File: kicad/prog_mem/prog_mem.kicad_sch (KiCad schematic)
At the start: 27 parts

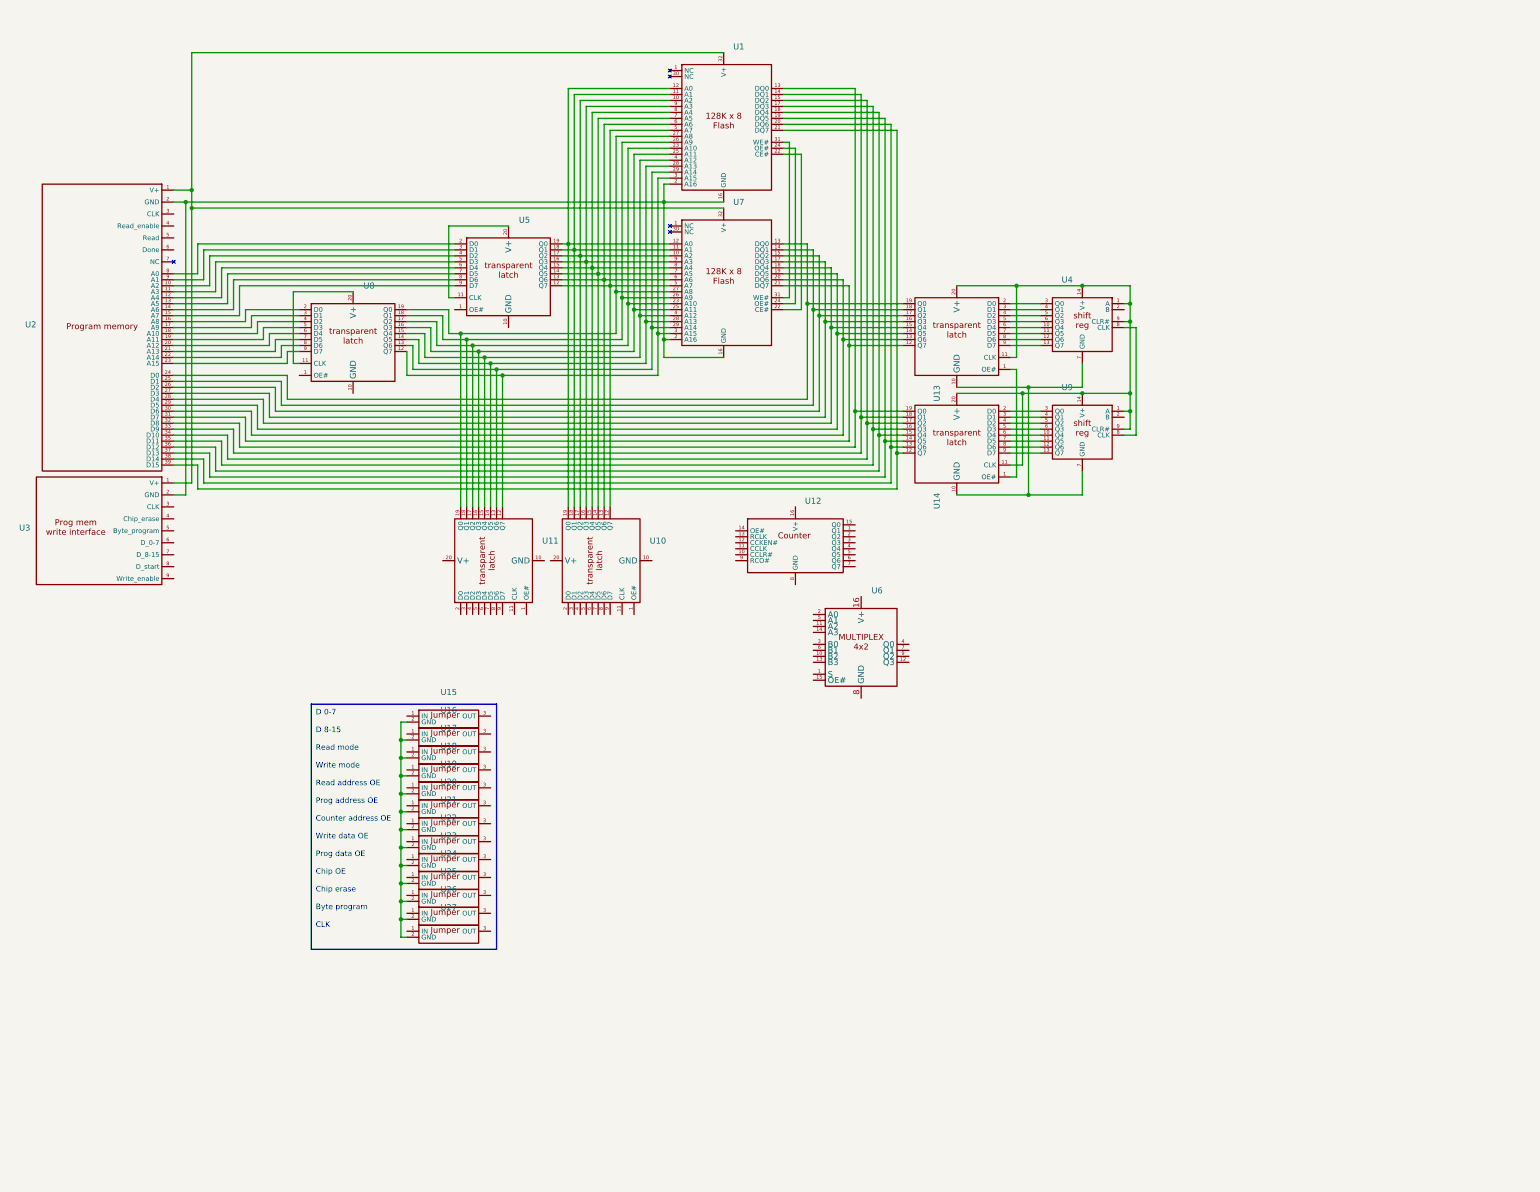
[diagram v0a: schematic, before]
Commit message: Finished some more PCBs and uploaded to JLCPCB
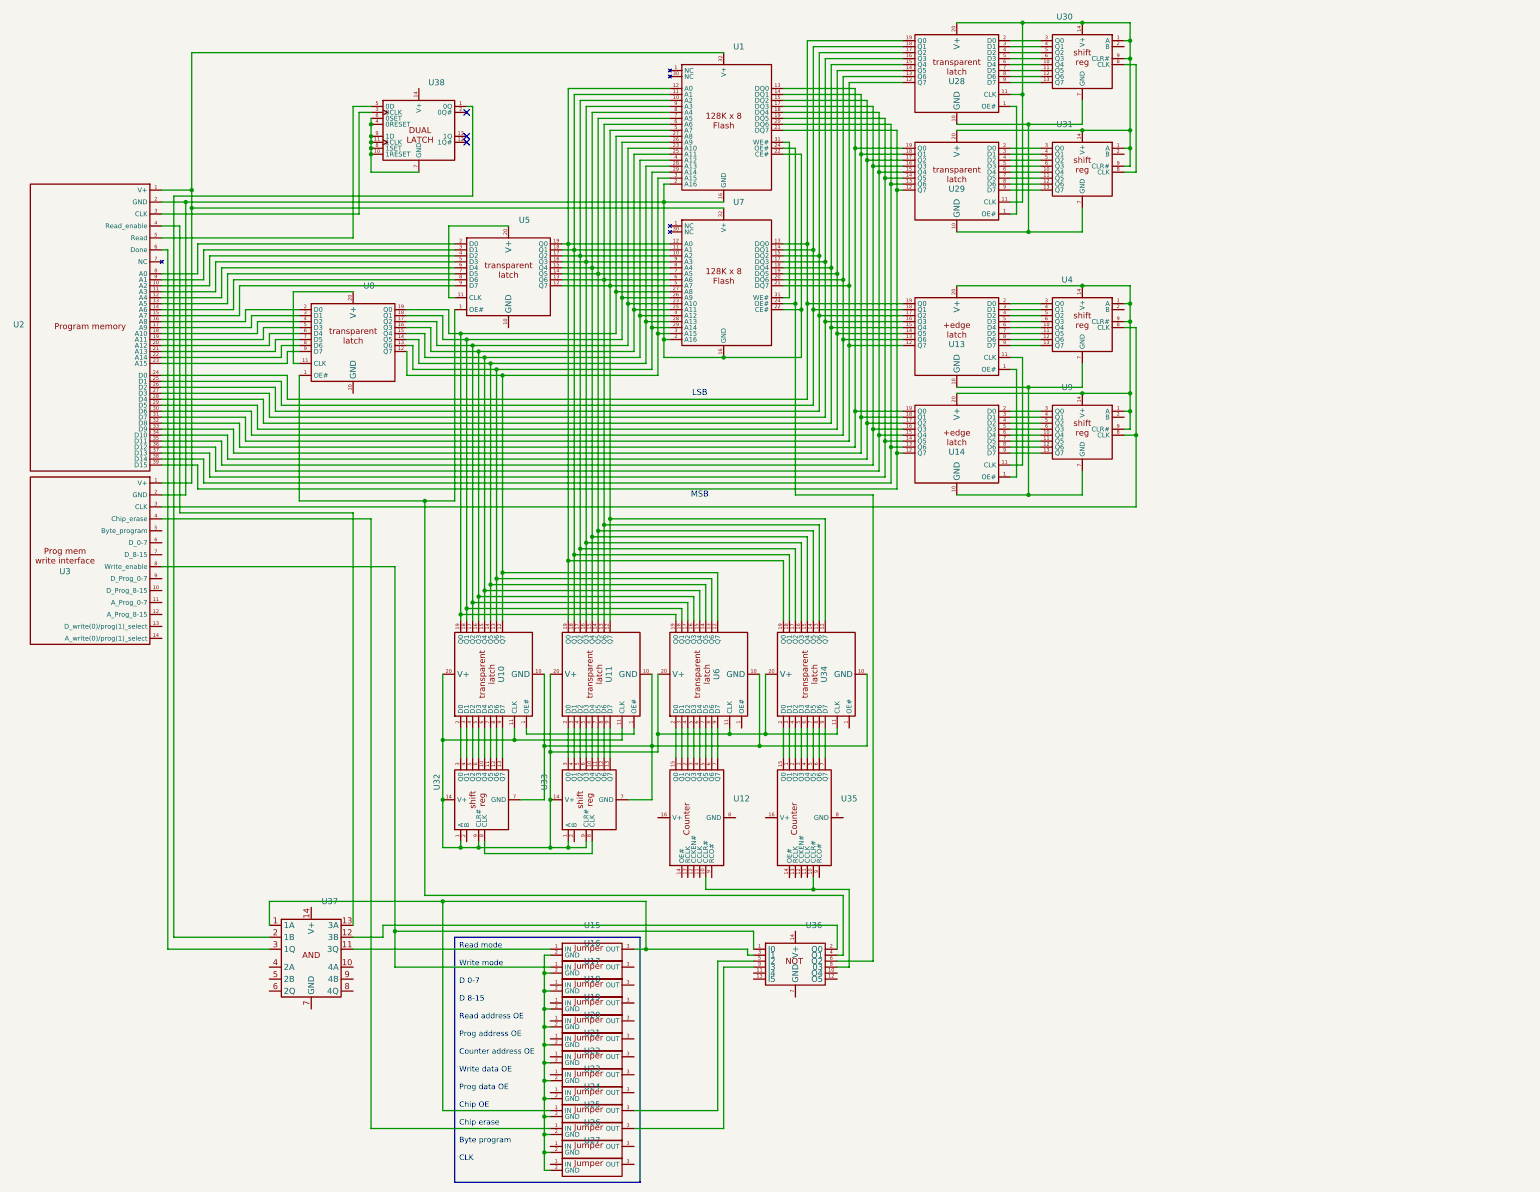
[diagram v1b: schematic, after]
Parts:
- removed U6: ~, Package_DIP:DIP-16_W7.62mm, symbol custom_symbol_lib:2x4_bit_multiplexer
- added U28, U29, U34, U6: ~, Package_DIP:DIP-20_W7.62mm, symbol custom_symbol_lib:8_bit_transparent_latch
- added U30, U31, U32, U33: ~, Package_DIP:DIP-14_W7.62mm, symbol custom_symbol_lib:8_bit_shift_register
- added U35: ~, Package_DIP:DIP-16_W7.62mm, symbol custom_symbol_lib:8_bit_counter
- added U36: ~, Package_DIP:DIP-14_W7.62mm, symbol custom_symbol_lib:6xNOT
- added U37: ~, Package_DIP:DIP-14_W7.62mm, symbol custom_symbol_lib:quad_and
- added U38: ~, Package_DIP:DIP-14_W7.62mm, symbol custom_symbol_lib:dual_latch
- U13, U14: symbol custom_symbol_lib:8_bit_transparent_latch -> custom_symbol_lib:rising_edge_8_bit_latch
- U3: footprint (none) -> Connector_PinHeader_2.54mm:PinHeader_1x08_P2.54mm_Horizontal
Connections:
- net at U12.1 (Q1): now also U6.3 (D1)
- net at U12.10 (CCLR#): now also U35.10 (CCLR#), U36.8 (03)
- net at U12.15 (Q0): now also U6.2 (D0)
- net at U12.2 (Q2): now also U6.4 (D2)
- net at U12.3 (Q3): now also U6.5 (D3)
- net at U12.4 (Q4): now also U6.6 (D4)
- net at U12.5 (Q5): now also U6.7 (D5)
- net at U12.6 (Q6): now also U6.8 (D6)
- net at U12.7 (Q7): now also U6.9 (D7)
- net at U25.1 (IN): now also U3.4 (Chip_erase)
- net at U25.3 (OUT): now also U36.9 (I3)
- net at U10.1 (OE#): now also U11.1 (OE#)
- net at U10.10 (GND): now also U11.10 (GND), U32.7 (GND), U33.7 (GND), U34.10 (GND), U6.10 (GND)
- net at U10.11 (CLK): now also U10.20 (V+), U11.11 (CLK), U11.20 (V+), U32.1 (A), U32.14 (V+), U32.9 (CLR#), U33.1 (A), U33.14 (V+), U33.9 (CLR#), U34.11 (CLK), U34.20 (V+), U6.11 (CLK), U6.20 (V+)
- net at U1.5 (A7), U5.12 (Q7), U7.5 (A7): now also U11.12 (Q7), U34.12 (Q7); no longer U10.12 (Q7)
- net at U1.6 (A6), U5.13 (Q6), U7.6 (A6): now also U11.13 (Q6), U34.13 (Q6); no longer U10.13 (Q6)
- net at U1.7 (A5), U5.14 (Q5), U7.7 (A5): now also U11.14 (Q5), U34.14 (Q5); no longer U10.14 (Q5)
- net at U1.8 (A4), U5.15 (Q4), U7.8 (A4): now also U11.15 (Q4), U34.15 (Q4); no longer U10.15 (Q4)
- net at U1.9 (A3), U5.16 (Q3), U7.9 (A3): now also U11.16 (Q3), U34.16 (Q3); no longer U10.16 (Q3)
- net at U1.10 (A2), U5.17 (Q2), U7.10 (A2): now also U11.17 (Q2), U34.17 (Q2); no longer U10.17 (Q2)
- net at U1.11 (A1), U5.18 (Q1), U7.11 (A1): now also U11.18 (Q1), U34.18 (Q1); no longer U10.18 (Q1)
- net at U1.12 (A0), U5.19 (Q0), U7.12 (A0): now also U11.19 (Q0), U34.19 (Q0); no longer U10.19 (Q0)
- net at U10.2 (D0): now also U32.3 (Q0)
- net at U10.3 (D1): now also U32.4 (Q1)
- net at U10.4 (D2): now also U32.5 (Q2)
- net at U10.5 (D3): now also U32.6 (Q3)
- net at U10.6 (D4): now also U32.10 (Q4)
- net at U10.7 (D5): now also U32.11 (Q5)
- net at U10.8 (D6): now also U32.12 (Q6)
- net at U10.9 (D7): now also U32.13 (Q7)
- net at U15.1 (IN): now also U37.11 (3Q)
- net at U15.3 (OUT): now also U24.1 (IN), U36.3 (I1), U37.1 (1A)
- net at U24.3 (OUT): now also U36.5 (I2)
- net at U1.13 (DQ0), U14.19 (Q0), U2.32 (D8): now also U29.19 (Q0)
- net at U1.14 (DQ1), U14.18 (Q1), U2.33 (D9): now also U29.18 (Q1)
- net at U1.15 (DQ2), U14.17 (Q2), U2.34 (D10): now also U29.17 (Q2)
- net at U1.16 (GND), U1.2 (A16), U2.2 (GND)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: now also U1.22 (CE#), U7.22 (CE#)
- net at U1.17 (DQ3), U14.16 (Q3), U2.35 (D11): now also U29.16 (Q3)
- net at U1.18 (DQ4), U14.15 (Q4), U2.36 (D12): now also U29.15 (Q4)
- net at U1.19 (DQ5), U14.14 (Q5), U2.37 (D13): now also U29.14 (Q5)
- net at U1.20 (DQ6), U14.13 (Q6), U2.38 (D14): now also U29.13 (Q6)
- net at U1.21 (DQ7), U14.12 (Q7), U2.39 (D15): now also U29.12 (Q7)
- net at U1.23 (A10), U7.23 (A10), U8.17 (Q2): now also U10.17 (Q2), U6.17 (Q2); no longer U11.17 (Q2)
- net at U1.24 (OE#), U7.24 (OE#): now also U36.6 (O2)
- net at U1.25 (A11), U7.25 (A11), U8.16 (Q3): now also U10.16 (Q3), U6.16 (Q3); no longer U11.16 (Q3)
- net at U1.26 (A9), U7.26 (A9), U8.18 (Q1): now also U10.18 (Q1), U6.18 (Q1); no longer U11.18 (Q1)
- net at U1.27 (A8), U7.27 (A8), U8.19 (Q0): now also U10.19 (Q0), U6.19 (Q0); no longer U11.19 (Q0)
- net at U1.28 (A13), U7.28 (A13), U8.14 (Q5): now also U10.14 (Q5), U6.14 (Q5); no longer U11.14 (Q5)
- net at U1.29 (A14), U7.29 (A14), U8.13 (Q6): now also U10.13 (Q6), U6.13 (Q6); no longer U11.13 (Q6)
- net at U1.3 (A15), U7.3 (A15), U8.12 (Q7): now also U10.12 (Q7), U6.12 (Q7); no longer U11.12 (Q7)
- net at U1.4 (A12), U7.4 (A12), U8.15 (Q4): now also U10.15 (Q4), U6.15 (Q4); no longer U11.15 (Q4)
- net at U13.20 (V+), U14.20 (V+), U4.1 (A)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: no longer U13.11 (CLK), U14.11 (CLK)
- net at U4.8 (CLK), U9.8 (CLK): now also U3.3 (CLK)
- net at U13.19 (Q0), U2.24 (D0), U7.13 (DQ0): now also U28.19 (Q0)
- net at U13.18 (Q1), U2.25 (D1), U7.14 (DQ1): now also U28.18 (Q1)
- net at U13.17 (Q2), U2.26 (D2), U7.15 (DQ2): now also U28.17 (Q2)
- net at U13.16 (Q3), U2.27 (D3), U7.17 (DQ3): now also U28.16 (Q3)
- net at U13.15 (Q4), U2.28 (D4), U7.18 (DQ4): now also U28.15 (Q4)
- net at U13.14 (Q5), U2.29 (D5), U7.19 (DQ5): now also U28.14 (Q5)
- net at U2.3 (CLK): now also U38.3 (0CLK)
- net at U13.13 (Q6), U2.30 (D6), U7.20 (DQ6): now also U28.13 (Q6)
- net at U13.12 (Q7), U2.31 (D7), U7.21 (DQ7): now also U28.12 (Q7)
- net at U2.4 (Read_enable): now also U37.13 (3A)
- net at U2.5 (Read): now also U38.5 (0D)
- net at U2.6 (Done): now also U37.3 (1Q)
- net at U5.1 (OE#): now also U8.1 (OE#), U36.4 (O1)
- net at U3.8 (Write_enable): now also U16.1 (IN), U36.1 (I0)
- net at U11.2 (D0): now also U33.3 (Q0)
- net at U11.3 (D1): now also U33.4 (Q1)
- net at U11.4 (D2): now also U33.5 (Q2)
- net at U11.5 (D3): now also U33.6 (Q3)
- net at U11.6 (D4): now also U33.10 (Q4)
- net at U11.7 (D5): now also U33.11 (Q5)
- net at U11.8 (D6): now also U33.12 (Q6)
- net at U11.9 (D7): now also U33.13 (Q7)
- new net: U34.2 (D0), U35.15 (Q0)
- new net: U34.3 (D1), U35.1 (Q1)
- new net: U34.4 (D2), U35.2 (Q2)
- new net: U34.5 (D3), U35.3 (Q3)
- new net: U34.6 (D4), U35.4 (Q4)
- new net: U34.7 (D5), U35.5 (Q5)
- new net: U34.8 (D6), U35.6 (Q6)
- new net: U34.9 (D7), U35.7 (Q7)
- new net: U37.2 (1B), U38.1 (0Q)
- new net: U38.10 (1RESET), U38.11 (1CLK), U38.4 (0RESET), U38.6 (0SET), U38.7 (GND), U38.8 (1SET), U38.9 (1D)
- new net: U28.1 (OE#), U29.1 (OE#)
- new net: U28.10 (GND), U29.10 (GND), U30.7 (GND), U31.7 (GND)
- new net: U28.11 (CLK), U28.20 (V+), U29.11 (CLK), U29.20 (V+), U30.1 (A), U30.14 (V+), U30.9 (CLR#), U31.1 (A), U31.14 (V+), U31.9 (CLR#)
- new net: U28.2 (D0), U30.3 (Q0)
- new net: U28.3 (D1), U30.4 (Q1)
- new net: U28.4 (D2), U30.5 (Q2)
- new net: U28.5 (D3), U30.6 (Q3)
- new net: U28.6 (D4), U30.10 (Q4)
- new net: U28.7 (D5), U30.11 (Q5)
- new net: U28.8 (D6), U30.12 (Q6)
- new net: U28.9 (D7), U30.13 (Q7)
- new net: U36.2 (O0), U37.12 (3B)
- new net: U29.6 (D4), U31.10 (Q4)
- new net: U29.7 (D5), U31.11 (Q5)
- new net: U29.8 (D6), U31.12 (Q6)
- new net: U29.9 (D7), U31.13 (Q7)
- new net: U29.2 (D0), U31.3 (Q0)
- new net: U29.3 (D1), U31.4 (Q1)
- new net: U29.4 (D2), U31.5 (Q2)
- new net: U29.5 (D3), U31.6 (Q3)
- new net: U30.8 (CLK), U31.8 (CLK)
- new net: U13.11 (CLK), U14.11 (CLK)
- new net: U32.8 (CLK), U33.8 (CLK)
- no-connect marks 0 -> 3
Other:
- note added: "LSB"
- note added: "MSB"
- moved on the sheet: U12, U15, U16, U17, U18, U19, U2, U20, U21, U22, U23, U24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

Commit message: Almost done with prog mem schematic
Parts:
- removed U19, U20, U21: ~, custom_footprint_library:jumper, symbol custom_symbol_lib:jumper
- added U39: ~, Package_DIP:DIP-14_W7.62mm, symbol custom_symbol_lib:quad_OR
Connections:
- net at U18.1 (IN): now also U3.7 (D_8-15)
- net at U18.3 (OUT): now also U9.2 (B)
- net at U34.1 (OE#): now also U23.3 (OUT), U35.11 (CCLK), U36.13 (I5), U6.1 (OE#)
- net at U22.1 (IN): now also U3.13 (D_write(0)/prog(1)_select)
- net at U27.1 (IN): now also U3.3 (CLK)
- net at U27.3 (OUT): now also U4.8 (CLK), U9.8 (CLK)
- net at U36.10 (O4): now also U39.13 (3B)
- net at U36.11 (I4): now also U16.3 (OUT)
- net at U36.12 (O5): now also U10.1 (OE#), U11.1 (OE#)
- net at U31.2 (B): now also U3.10 (D_Prog_8-15)
- net at U1.31 (WE#), U7.31 (WE#): now also U26.3 (OUT)
- net at U4.2 (B): now also U17.3 (OUT)
- net at U3.11 (A_Prog_0-7): now also U33.2 (B)
- net at U3.12 (A_Prog_8-15): now also U32.2 (B)
- net at U3.14 (A_write(0)/prog(1)_select): now also U23.1 (IN)
- net at U3.5 (WE#): now also U39.12 (3A)
- net at U3.6 (D_0-7): now also U17.1 (IN)
- net at U3.9 (D_Prog_0-7): now also U30.2 (B)
- net at U26.1 (IN): now also U39.11 (Q3)
- new net: U39.1 (0A), U39.2 (0B), U39.5 (1A), U39.6 (1B), U39.7 (GND), U39.8 (2A), U39.9 (2B)
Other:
- note added: "Data - Program"
- note added: "Data - Write"
- moved on the sheet: U22, U23, U24, U25, U26, U27

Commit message: Finished prog mem schematic
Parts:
- removed U12, U35: ~, Package_DIP:DIP-16_W7.62mm, symbol custom_symbol_lib:8_bit_counter
- removed U16, U26, U27: ~, custom_footprint_library:jumper, symbol custom_symbol_lib:jumper
- removed U28, U29, U34, U6: ~, Package_DIP:DIP-20_W7.62mm, symbol custom_symbol_lib:8_bit_transparent_latch
- removed U30, U31: ~, Package_DIP:DIP-14_W7.62mm, symbol custom_symbol_lib:8_bit_shift_register
- removed U36: ~, Package_DIP:DIP-14_W7.62mm, symbol custom_symbol_lib:6xNOT
- removed U37: ~, Package_DIP:DIP-14_W7.62mm, symbol custom_symbol_lib:quad_and
- removed U39: ~, Package_DIP:DIP-14_W7.62mm, symbol custom_symbol_lib:quad_OR
- added D1: D, Diode_THT:D_A-405_P7.62mm_Horizontal, symbol Device:D
- added R1, R10, R2, R3, R4, R5, R6, R7, R8, R9: 10k, custom_footprint_library:0.4_pitch_resistor, symbol Device:R
- added U12: ~, Package_DIP:DIP-14_W7.62mm, symbol custom_symbol_lib:6xNOT
- added U19: ~, Connector_PinHeader_2.54mm:PinHeader_1x16_P2.54mm_Vertical, symbol custom_symbol_lib:connector_16_bit
- added U20: ~, custom_footprint_library:jumper, symbol custom_symbol_lib:jumper
- added U6: ~, Package_DIP:DIP-14_W7.62mm, symbol custom_symbol_lib:quad_and
- U13, U14: symbol custom_symbol_lib:rising_edge_8_bit_latch -> custom_symbol_lib:8_bit_transparent_latch
- U3: footprint Connector_PinHeader_2.54mm:PinHeader_1x08_P2.54mm_Horizontal -> Connector_PinHeader_2.54mm:PinHeader_1x10_P2.54mm_Horizontal
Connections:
- net at U18.1 (IN): now also U3.5 (D_0-7), R2.2; no longer U3.7 (D_8-15)
- net at U15.2 (GND), U17.2 (GND), U18.2 (GND)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: now also U1.16 (GND), U1.2 (A16), U1.22 (CE#), U10.10 (GND), U11.10 (GND), U13.10 (GND), U14.10 (GND), U2.2 (GND), U3.2 (GND), U32.7 (GND), U33.7 (GND), U38.10 (1RESET), U38.11 (1CLK), U38.4 (0RESET), U38.6 (0SET), U38.7 (GND), U38.8 (1SET), U38.9 (1D), U4.7 (GND), U5.10 (GND), U7.16 (GND), U7.2 (A16), U7.22 (CE#), U8.10 (GND), U9.7 (GND), R1.1, R10.1, R2.1, R3.1, R4.1, R5.1, R6.1, R7.1, R9.1, U12.11 (I4), U12.13 (I5), U12.7 (GND), U12.9 (I3), U20.2 (GND), U6.10 (4A), U6.12 (3B), U6.13 (3A), U6.7 (GND), U6.9 (4B)
- net at U18.3 (OUT): now also U4.2 (B); no longer U9.2 (B)
- net at U23.3 (OUT): now also U33.2 (B)
- net at U10.11 (CLK), U10.20 (V+), U11.11 (CLK)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: now also U1.32 (V+), U13.11 (CLK), U13.20 (V+), U14.11 (CLK), U14.20 (V+), U3.1 (V+), U38.14 (V+), U4.1 (A), U4.14 (V+), U4.9 (CLR#), U5.11 (CLK), U5.20 (V+), U7.32 (V+), U8.11 (CLK), U8.20 (V+), U9.1 (A), U9.14 (V+), U9.9 (CLR#), D1.1 (K), R8.1, U12.14 (V+), U6.14 (V+)
- net at U1.5 (A7), U11.12 (Q7), U5.12 (Q7)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: now also U19.8 (7)
- net at U1.6 (A6), U11.13 (Q6), U5.13 (Q6)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: now also U19.7 (6)
- net at U1.7 (A5), U11.14 (Q5), U5.14 (Q5)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: now also U19.6 (5)
- net at U1.8 (A4), U11.15 (Q4), U5.15 (Q4)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: now also U19.5 (4)
- net at U1.9 (A3), U11.16 (Q3), U5.16 (Q3)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: now also U19.4 (3)
- net at U1.10 (A2), U11.17 (Q2), U5.17 (Q2)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: now also U19.3 (2)
- net at U1.11 (A1), U11.18 (Q1), U5.18 (Q1)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: now also U19.2 (1)
- net at U1.12 (A0), U11.19 (Q0), U5.19 (Q0)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: now also U19.1 (0)
- net at U25.1 (IN): now also U15.3 (OUT), U6.5 (2B); no longer U3.4 (Addr_counter_CLR)
- net at U25.3 (OUT): now also U12.3 (I1)
- net at U38.1 (0Q): now also U6.4 (2A)
- net at U2.3 (CLK), U38.3 (0CLK): now also R9.2
- net at U2.5 (Read), U38.5 (0D): now also R10.2
- net at U22.1 (IN): now also U3.6 (D_8-15), R3.2; no longer U3.13 (D_write(0)/prog(1)_select)
- net at U22.3 (OUT): now also U9.2 (B)
- net at U15.1 (IN): now also U6.3 (1Q)
- net at U24.1 (IN): now also U3.9 (A_8-15), R6.2; no longer U15.3 (OUT)
- net at U3.3 (Write_mode_enable): now also U17.1 (IN), R1.2
- net at U4.8 (CLK), U9.8 (CLK): now also U3.7 (D_CLK), R4.2
- net at U3.8 (A_0-7): now also U23.1 (IN), R5.2
- net at U10.1 (OE#), U11.1 (OE#): now also U13.1 (OE#), U14.1 (OE#), U12.6 (O2)
- net at U5.1 (OE#), U8.1 (OE#): now also U1.24 (OE#), U7.24 (OE#), U12.4 (O1)
- net at U24.3 (OUT): now also U32.2 (B)
- net at U3.10 (A_CLK): now also U32.8 (CLK), U33.8 (CLK), R7.2
- net at U1.23 (A10), U10.17 (Q2), U7.23 (A10)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: now also U19.11 (10)
- net at U1.25 (A11), U10.16 (Q3), U7.25 (A11)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: now also U19.12 (11)
- net at U1.26 (A9), U10.18 (Q1), U7.26 (A9)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: now also U19.10 (9)
- net at U1.27 (A8), U10.19 (Q0), U7.27 (A8)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: now also U19.9 (8)
- net at U1.28 (A13), U10.14 (Q5), U7.28 (A13)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: now also U19.14 (13)
- net at U1.29 (A14), U10.13 (Q6), U7.29 (A14)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: now also U19.15 (14)
- net at U1.3 (A15), U10.12 (Q7), U7.3 (A15)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: now also U19.16 (15)
- net at U1.31 (WE#), U7.31 (WE#): now also U3.4 (WE#), R8.2
- net at U1.4 (A12), U10.15 (Q4), U7.4 (A12)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: now also U19.13 (12)
- net at U2.4 (Read_enable): now also U6.1 (1A)
- net at U2.6 (Done): now also U6.6 (2Q)
- net at U17.3 (OUT): now also U12.1 (I0), U20.1 (IN); no longer U4.2 (B)
- new net: U12.2 (O0), U6.2 (1B)
- new net: U12.5 (I2), U20.3 (OUT)
- new net: D1.2 (A), U2.1 (V+)
- no-connect marks 3 -> 8
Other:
- note removed: "Data - Program"
- note removed: "Data - Write"
- moved on the sheet: U1, U10, U11, U13, U14, U15, U17, U18, U2, U22, U23, U24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
